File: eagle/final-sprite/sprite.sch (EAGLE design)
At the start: 60 parts, among them J1 M20-7910442R, U1 CC430F513X, U2 LSM9DS1, U4 DRV8837, U5 ADP5092, U6 DRV8837, U7 DRV8837, X1 SPRITEPIN_SPRITE_PIN, X2 SPRITEPIN_SPRITE_PIN

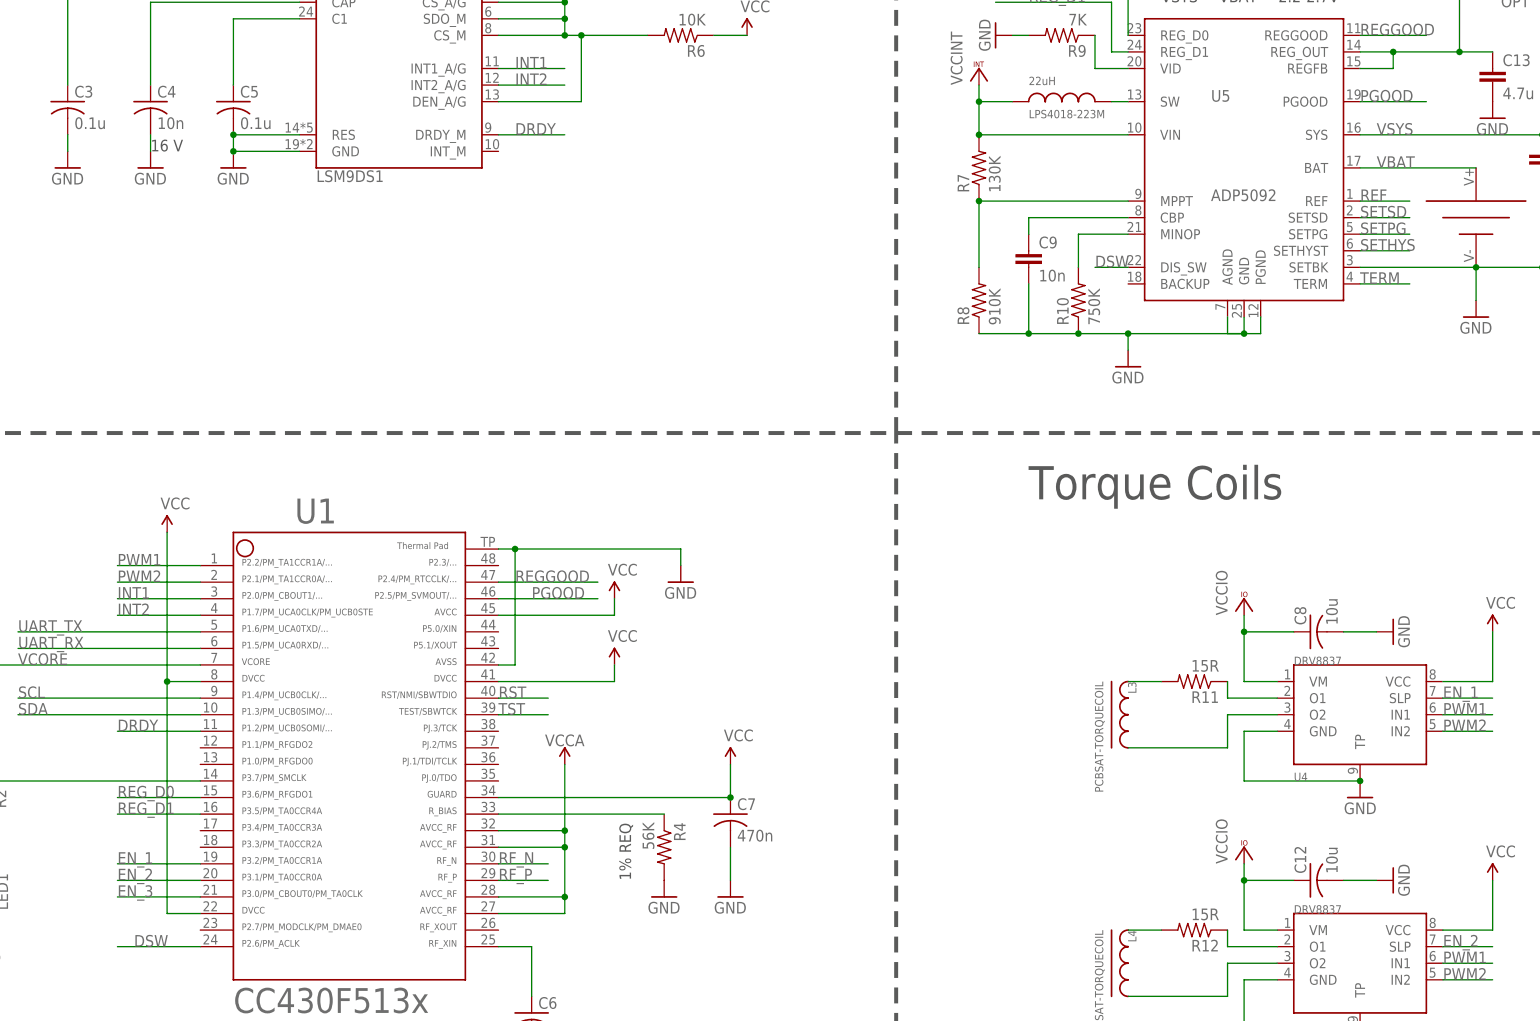
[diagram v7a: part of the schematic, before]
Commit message: did most of the long traces
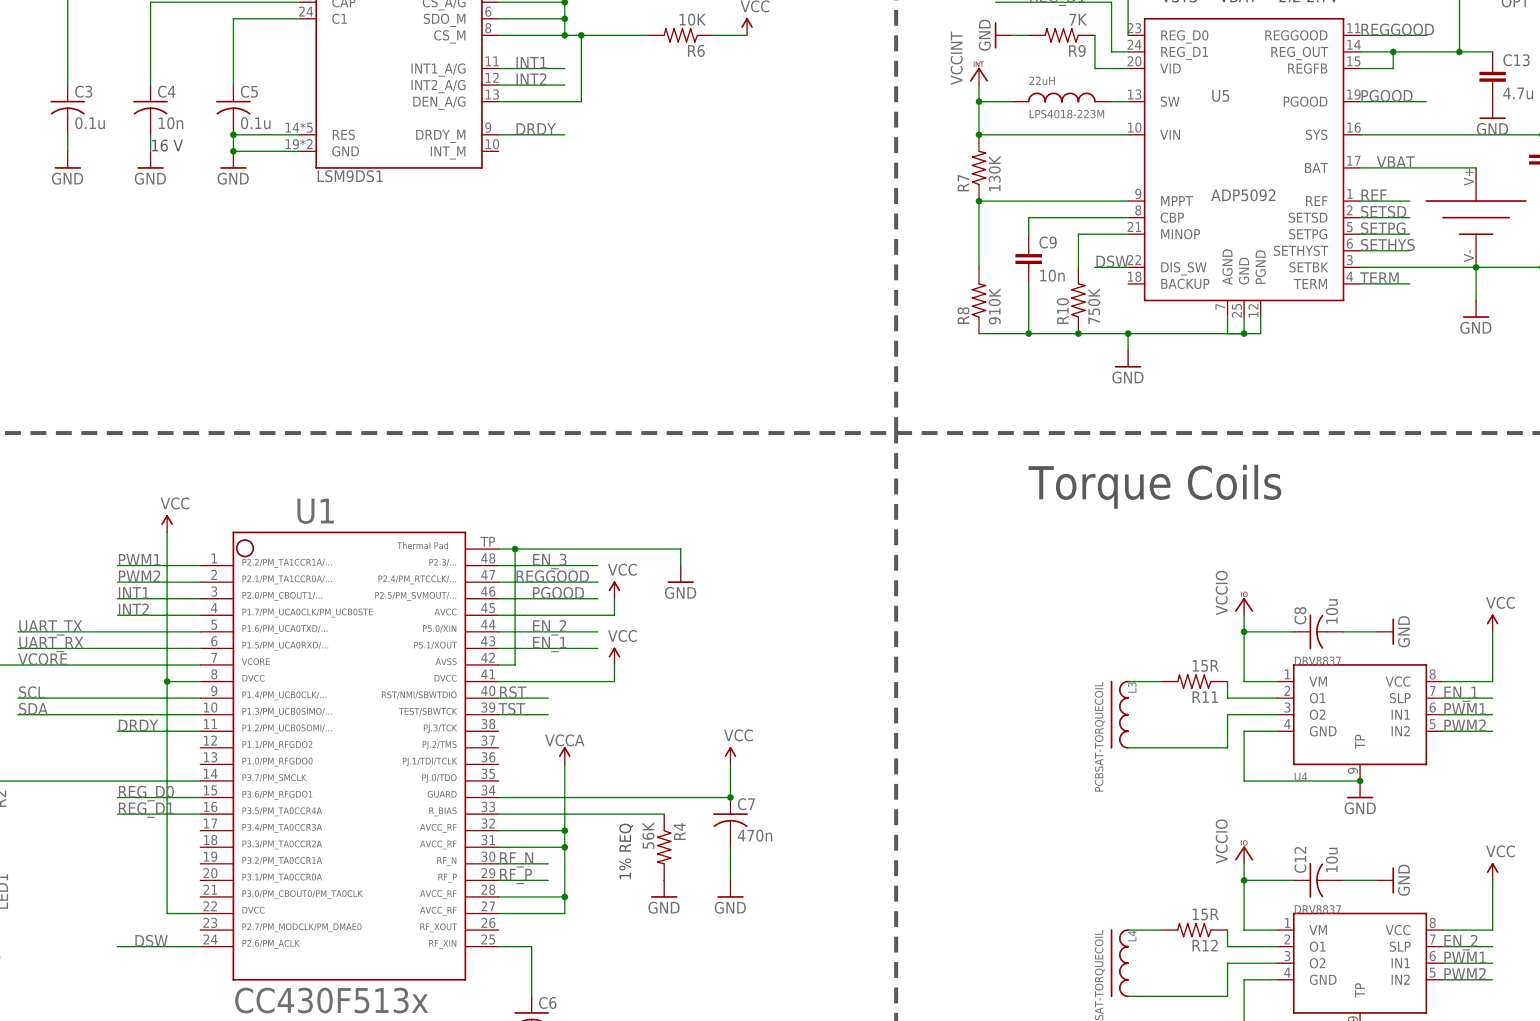
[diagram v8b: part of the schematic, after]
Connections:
- removed net VSYS: C14.1, C15.1, R13.2, R14.1, U5.SYS
- net EN_1: now also U1.43; no longer U1.19
- net EN_2: now also U1.44; no longer U1.20
- net EN_3: now also U1.48; no longer U1.21
- net VCC: now also C14.1, C15.1, R13.2, R14.1, U5.SYS
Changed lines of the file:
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@@
 <pinref part="R1" gate="G$1" pin="1"/>
+</segment>
+<segment>
+<pinref part="U5" gate="G$1" pin="SYS"/>
+<wire x1="157.48" y1="-121.92" x2="185.42" y2="-121.92" width="0.1524" layer="91"/>
+<wire x1="185.42" y1="-121.92" x2="193.04" y2="-121.92" width="0.1524" layer="91"/>
+<wire x1="193.04" y1="-121.92" x2="193.04" y2="-99.06" width="0.1524" layer="91"/>
+<pinref part="P+12" gate="1" pin="VCC"/>
+<pinref part="C14" gate="G$1" pin="1"/>
+<junction x="185.42" y="-121.92"/>
+<pinref part="C15" gate="G$1" pin="1"/>
+<junction x="193.04" y="-121.92"/>
+<wire x1="193.04" y1="-99.06" x2="193.04" y2="-88.9" width="0.1524" layer="91"/>
+<junction x="193.04" y="-99.06"/>
+<pinref part="R14" gate="G$1" pin="1"/>
+<wire x1="193.04" y1="-99.06" x2="198.12" y2="-99.06" width="0.1524" layer="91"/>
+<pinref part="R13" gate="G$1" pin="2"/>
+<wire x1="187.96" y1="-99.06" x2="193.04" y2="-99.06" width="0.1524" layer="91"/>
 </segment>
 </net>
@@
 </segment>
 <segment>
-<pinref part="U1" gate="G$1" pin="19"/>
-<wire x1="-20.32" y1="-233.68" x2="-33.02" y2="-233.68" width="0.1524" layer="91"/>
-<label x="-33.02" y="-233.68" size="1.778" layer="95"/>
+<pinref part="U1" gate="G$1" pin="43"/>
+<wire x1="25.4" y1="-200.66" x2="40.64" y2="-200.66" width="0.1524" layer="91"/>
+<label x="30.48" y="-200.66" size="1.778" layer="95"/>
 </segment>
 </net>
@@
 </segment>
 <segment>
-<pinref part="U1" gate="G$1" pin="20"/>
-<wire x1="-20.32" y1="-236.22" x2="-33.02" y2="-236.22" width="0.1524" layer="91"/>
-<label x="-33.02" y="-236.22" size="1.778" layer="95"/>
+<pinref part="U1" gate="G$1" pin="44"/>
+<wire x1="25.4" y1="-198.12" x2="40.64" y2="-198.12" width="0.1524" layer="91"/>
+<label x="30.48" y="-198.12" size="1.778" layer="95"/>
 </segment>
 </net>
@@
 </segment>
 <segment>
-<pinref part="U1" gate="G$1" pin="21"/>
-<wire x1="-20.32" y1="-238.76" x2="-33.02" y2="-238.76" width="0.1524" layer="91"/>
-<label x="-33.02" y="-238.76" size="1.778" layer="95"/>
+<pinref part="U1" gate="G$1" pin="48"/>
+<wire x1="25.4" y1="-187.96" x2="40.64" y2="-187.96" width="0.1524" layer="91"/>
+<label x="30.48" y="-187.96" size="1.778" layer="95"/>
 </segment>
 </net>
@@
 </segment>
 </net>
-<net name="VSYS" class="0">
-<segment>
-<pinref part="U5" gate="G$1" pin="SYS"/>
-<wire x1="157.48" y1="-121.92" x2="185.42" y2="-121.92" width="0.1524" layer="91"/>
-<wire x1="185.42" y1="-121.92" x2="193.04" y2="-121.92" width="0.1524" layer="91"/>
-<wire x1="193.04" y1="-121.92" x2="193.04" y2="-99.06" width="0.1524" layer="91"/>
-<pinref part="P+12" gate="1" pin="VCC"/>
-<pinref part="C14" gate="G$1" pin="1"/>
-<junction x="185.42" y="-121.92"/>
-<pinref part="C15" gate="G$1" pin="1"/>
-<junction x="193.04" y="-121.92"/>
-<wire x1="193.04" y1="-99.06" x2="193.04" y2="-88.9" width="0.1524" layer="91"/>
-<junction x="193.04" y="-99.06"/>
-<pinref part="R14" gate="G$1" pin="1"/>
-<wire x1="193.04" y1="-99.06" x2="198.12" y2="-99.06" width="0.1524" layer="91"/>
-<label x="160.02" y="-121.92" size="1.778" layer="95"/>
-<pinref part="R13" gate="G$1" pin="2"/>
-<wire x1="187.96" y1="-99.06" x2="193.04" y2="-99.06" width="0.1524" layer="91"/>
-</segment>
-</net>
